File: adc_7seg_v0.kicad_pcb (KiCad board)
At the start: 4 copper layers, 34 parts, among them J1 IN, J2 DC, Q1 BC847, U1 MC78M09C, U2 ICL7106, U3 TDSR1350, U4 TDSR1350, U5 TDSR1350

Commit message: Deployed the remaining parts RC
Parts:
- C3, C6, C7, C8, C9, JP4, Q1, R10, R11, R12: moved to B.Cu
- moved R12 37.3 mm to (192.4, 91.8), turned to 90 degrees
- moved R13 34.5 mm to (220.7, 88.3), turned to 270 degrees
- moved C3 31.3 mm to (210.4, 88.1), turned to 180 degrees
- moved C6 29.6 mm to (221.1, 98.2), turned to 270 degrees
- moved C7 29.0 mm to (224.0, 98.2), turned to 270 degrees
- moved R11 27.1 mm to (210.4, 89.7), turned to 180 degrees
- moved JP4 25.1 mm to (192.4, 94.6)
- moved C8 21.6 mm to (210.4, 91.2), turned to 180 degrees
- moved C9 16.1 mm to (216.7, 98.2), turned to 90 degrees
- moved R10 15.2 mm to (222.6, 98.2), turned to 270 degrees
- moved C5 0.83 mm to (218.9, 97.4)
- moved Q1 0.11 mm to (206.6, 94.2), turned to 90 degrees
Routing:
- net Net-(U2-Pad9): track 17.6 -> 0.00 mm, vias 2 -> 0
- net Net-(U2-Pad10): track 14.4 -> 0.00 mm
- net Net-(U2-Pad21): track 41.5 -> 45.1 mm
- net Net-(U2-Pad25): track 62.7 -> 61.6 mm

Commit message: Revert "Deployed the remaining parts RC"
This reverts commit 7c6476d39b73f4d8eff57732889eea5eef9e1166.
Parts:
- C3, C6, C7, C8, C9, JP4, Q1, R10, R11, R12: moved to F.Cu
- moved R12 37.3 mm to (225.1, 109.6), turned to 0 degrees
- moved R13 34.5 mm to (212.1, 121.7), turned to 0 degrees
- moved C3 31.3 mm to (214.2, 119.2), turned to 0 degrees
- moved C6 29.6 mm to (204.1, 122.4), turned to 0 degrees
- moved C7 29.0 mm to (208.1, 122.4), turned to 0 degrees
- moved R11 27.1 mm to (229.1, 109.3), turned to 0 degrees
- moved JP4 25.1 mm to (200.5, 118.3)
- moved C8 21.6 mm to (225.1, 107.1), turned to 0 degrees
- moved C9 16.1 mm to (230.3, 106.8), turned to 0 degrees
- moved R10 15.2 mm to (237.4, 101.5), turned to 0 degrees
- moved C5 0.83 mm to (219.7, 97.4)
- moved Q1 0.11 mm to (206.5, 94.2), turned to 0 degrees
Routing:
- net Net-(U2-Pad9): track 0.00 -> 17.6 mm, vias 0 -> 2
- net Net-(U2-Pad10): track 0.00 -> 14.4 mm
- net Net-(U2-Pad21): track 45.1 -> 41.5 mm
- net Net-(U2-Pad25): track 61.6 -> 62.7 mm

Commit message: first pokus backup
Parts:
- U2: footprint Package_QFP:LQFP-44_10x10mm_P0.8mm -> Package_QFP:TQFP-44_10x10mm_P0.8mm
- U3, U4, U5: footprint KLALIB_Display_7Segment:TDSR1350 -> KLALIB_Display_7Segment:TDSR1350_small_pads
- moved U2 24.7 mm to (194.3, 90.5), turned to 180 degrees
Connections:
- U3 pad 8: Net-(U3-Pad8) -> (no net)
- U4 pad 8: Net-(U4-Pad8) -> (no net)
- U5 pad 5: Net-(U5-Pad5) -> (no net)
- U5 pad 8: Net-(U5-Pad8) -> (no net)
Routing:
- net Net-(U2-Pad29): track 67.3 -> 0.00 mm
- net Net-(U2-Pad25): track 62.7 -> 0.00 mm, vias 2 -> 0
- net Net-(U2-Pad24): track 59.7 -> 0.00 mm
- net Net-(U2-Pad31): track 56.9 -> 0.00 mm
- net Net-(U2-Pad22): track 52.8 -> 0.00 mm, vias 2 -> 0
- net Net-(U2-Pad23): track 45.8 -> 0.00 mm
- net Net-(U2-Pad30): track 45.2 -> 0.00 mm, vias 1 -> 0
- net Net-(U2-Pad32): track 42.8 -> 0.00 mm, vias 1 -> 0
- net Net-(U2-Pad21): track 41.5 -> 0.00 mm, vias 2 -> 0
- net Net-(U2-Pad20): track 36.0 -> 0.00 mm
- net Net-(U2-Pad19): track 29.5 -> 0.00 mm
- net Net-(U2-Pad18): track 25.1 -> 0.00 mm
- net Net-(U2-Pad15): track 19.6 -> 0.00 mm, vias 1 -> 0
- net Net-(U2-Pad14): track 19.4 -> 0.00 mm
- net Net-(U2-Pad9): track 17.6 -> 0.00 mm, vias 2 -> 0
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
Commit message: updated gitgnore, some changes, wip
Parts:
- C6, C7, C8, C9, R10, R11: moved to B.Cu
- moved R12 82.5 mm to (142.6, 110.6)
- moved JP4 57.6 mm to (143.1, 113.4)
- moved R10 53.5 mm to (184.5, 94.1), turned to 180 degrees
- moved C9 49.6 mm to (185.0, 86.5), turned to 270 degrees
- moved R11 44.5 mm to (193.3, 82.9)
- moved R13 42.6 mm to (219.6, 79.8)
- moved C8 41.2 mm to (193.2, 81.0)
- moved C6 36.0 mm to (184.5, 92.1), turned to 180 degrees
- moved C7 35.8 mm to (184.2, 95.6), turned to 180 degrees
- moved C5 35.4 mm to (185.1, 89.9), turned to 90 degrees
- moved C3 24.5 mm to (218.4, 95.0)
- moved U2 1.46 mm to (192.8, 90.5), turned to 270 degrees
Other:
- net class Default: clearance 0.2 -> 0.254; trace_width 0.25 -> 0.254
- rule trace_clearance: 0.2 -> 0.254

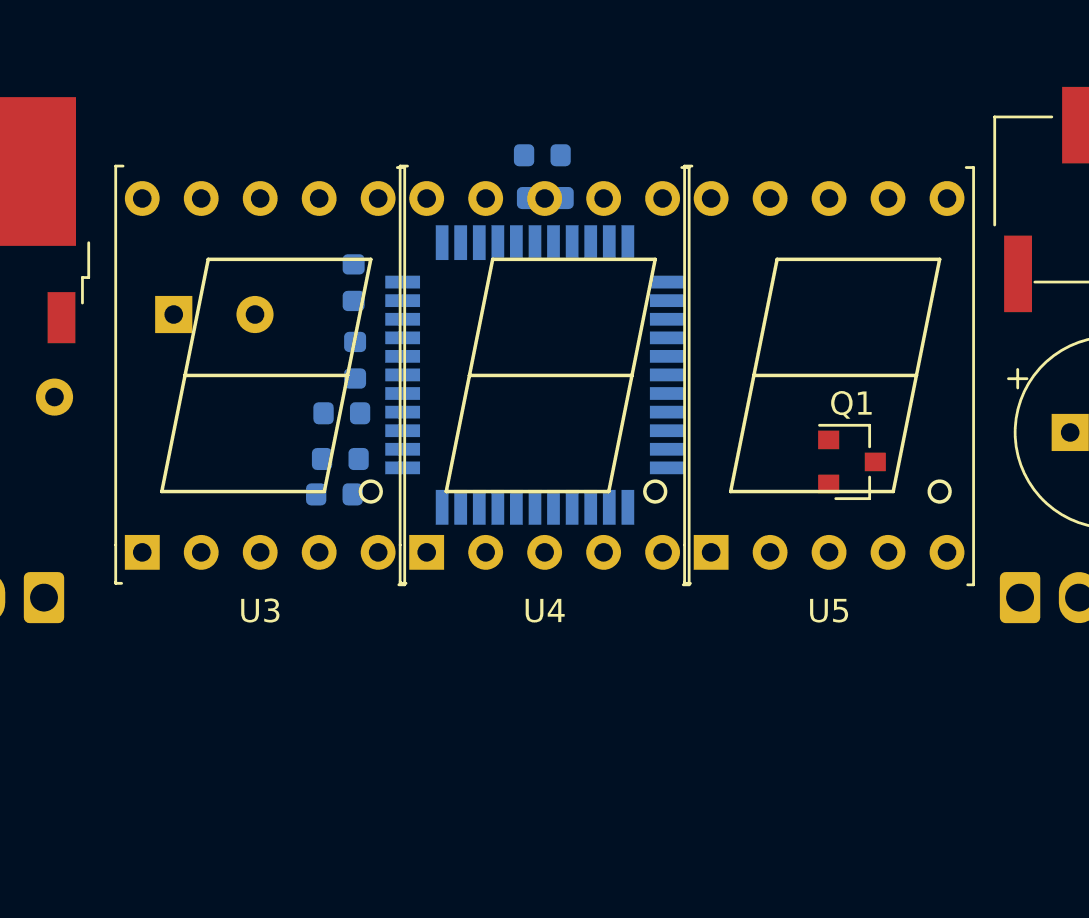
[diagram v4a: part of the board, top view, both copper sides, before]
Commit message: first pokus most of via
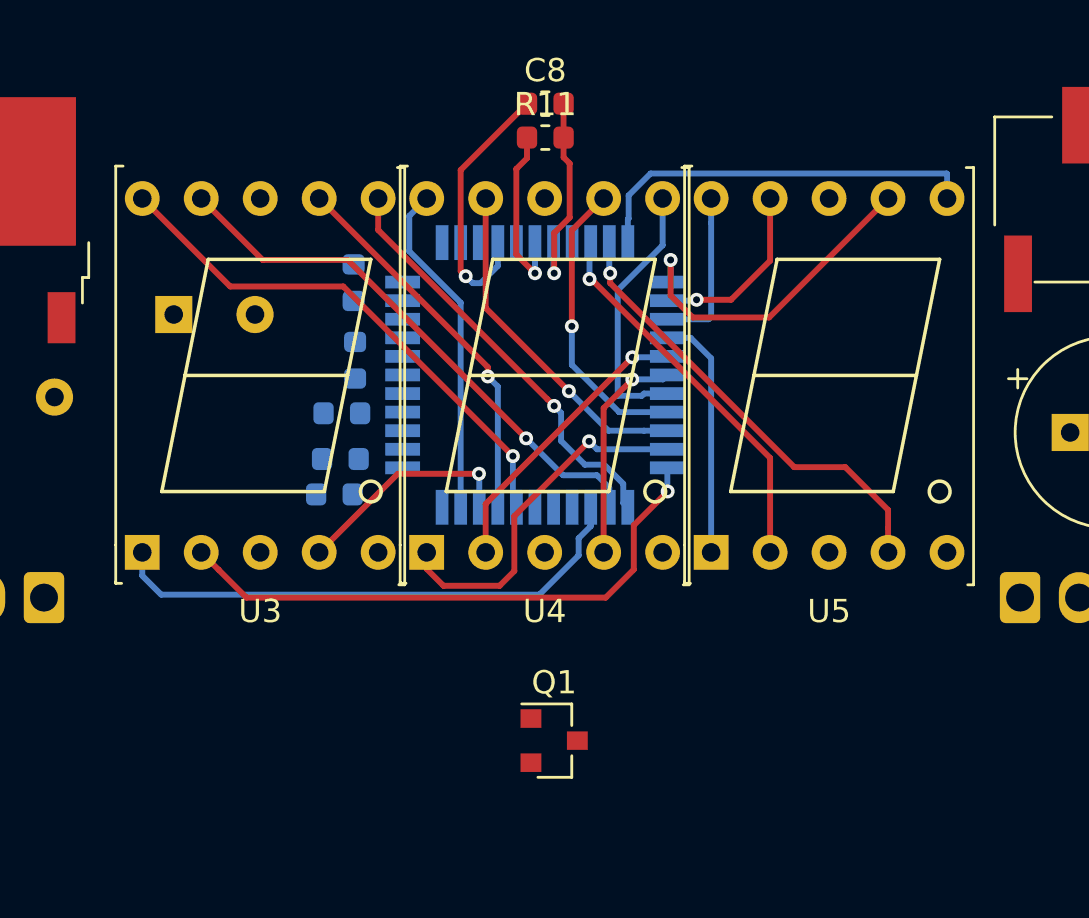
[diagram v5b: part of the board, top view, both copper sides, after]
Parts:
- C8, R11: moved to F.Cu
- moved Q1 17.6 mm to (193.7, 106.2)
- moved R11 2.60 mm to (193.3, 80.3)
- moved C8 2.23 mm to (193.3, 78.8)
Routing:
- net Net-(U2-Pad22): track 0.00 -> 24.9 mm, vias 0 -> 1
- net Net-(U2-Pad24): track 0.00 -> 23.6 mm, vias 0 -> 1
- net Net-(U2-Pad25): track 0.00 -> 23.1 mm
- net Net-(U2-Pad29): track 0.00 -> 22.8 mm, vias 0 -> 1
- net Net-(U2-Pad10): track 0.00 -> 19.6 mm, vias 0 -> 1
- net Net-(U2-Pad23): track 0.00 -> 18.2 mm, vias 0 -> 1
- net Net-(U2-Pad11): track 0.00 -> 17.2 mm
- net Net-(U2-Pad9): track 0.00 -> 16.6 mm, vias 0 -> 1
- net Net-(U2-Pad30): track 0.00 -> 16.5 mm, vias 0 -> 1
- net Net-(U2-Pad21): track 0.00 -> 15.5 mm, vias 0 -> 1
- net Net-(U2-Pad20): track 0.00 -> 14.7 mm, vias 0 -> 1
- net Net-(U2-Pad32): track 0.00 -> 14.5 mm
- net Net-(U2-Pad12): track 0.00 -> 14.4 mm, vias 0 -> 1
- net Net-(U2-Pad19): track 0.00 -> 12.7 mm, vias 0 -> 1
- net Net-(U2-Pad16): track 0.00 -> 12.5 mm, vias 0 -> 1
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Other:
- net class Default: clearance 0.254 -> 0.2
- rule trace_clearance: 0.254 -> 0.2

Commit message: almost last version 0.2.2
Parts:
- removed C4: 100u, Capacitor_THT:CP_Radial_D8.0mm_P3.50mm
- JP1, JP2, JP3: footprint Jumper:SolderJumper-2_P1.3mm_Open_Pad1.0x1.5mm -> KLIB_Mechanical:Jumper; moved to B.Cu
- JP4, R1, R12, R13, R2, R3, R4, R5, R6, R7, R8, U1: moved to B.Cu
- RV1: footprint KLALIB_Potenciometer_SMD:Potentiometer_Bourns_3269P_Horizontal -> KLALIB_Potenciometer_SMD:Potentiometer_SRPASSIVES_1801; moved to B.Cu
- moved JP4 51.4 mm to (193.0, 100.8)
- moved R12 47.4 mm to (189.1, 101.9), turned to 180 degrees
- moved R2 42.1 mm to (184.8, 96.0), turned to 0 degrees
- moved R6 40.8 mm to (184.8, 94.6), turned to 0 degrees
- moved R5 40.0 mm to (184.1, 92.3), turned to 270 degrees
- moved R7 39.3 mm to (188.1, 94.7), turned to 0 degrees
- moved R1 38.1 mm to (185.6, 92.3), turned to 270 degrees
- moved JP3 37.7 mm to (187.9, 93.1), turned to 0 degrees
- moved R4 37.5 mm to (184.8, 90.1), turned to 0 degrees
- moved R3 36.6 mm to (184.8, 88.6), turned to 180 degrees
- moved JP2 35.4 mm to (187.9, 91.5), turned to 0 degrees
- moved R13 35.2 mm to (184.7, 84.7), turned to 180 degrees
- moved R8 34.2 mm to (190.6, 90.0), turned to 90 degrees
- moved J1 34.1 mm to (179.8, 96.1), turned to 90 degrees
- moved JP1 33.5 mm to (187.8, 89.4), turned to 0 degrees
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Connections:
- U2 pad 26: Net-(U2-Pad26) -> (no net)
- U2 pad 27: Net-(U2-Pad27) -> (no net)
- U2 pad 3: Net-(U2-Pad3) -> (no net)
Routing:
- net +9V: track 0.00 -> 94.0 mm, vias 0 -> 3
- net Net-(C5-Pad2): track 0.00 -> 35.9 mm
- net Net-(Q1-Pad2): track 0.00 -> 29.0 mm
- net Net-(U2-Pad25): track 23.1 -> 50.4 mm, vias 0 -> 1
- net Net-(U2-Pad18): track 11.5 -> 32.1 mm
- net Net-(U2-Pad14): track 7.02 -> 25.2 mm
- net Net-(U2-Pad22): track 24.9 -> 38.2 mm, vias 1 -> 0
- net Net-(C1-Pad1): track 0.00 -> 13.3 mm
- net Net-(J1-Pad2): track 0.00 -> 12.9 mm
- net Net-(U2-Pad21): track 15.5 -> 27.1 mm
- net Net-(U2-Pad13): track 7.82 -> 19.3 mm, vias 1 -> 0
- net Net-(U2-Pad29): track 22.8 -> 32.1 mm
- net Net-(Q1-Pad1): track 0.00 -> 9.13 mm, vias 0 -> 1
- net Net-(U2-Pad12): track 14.4 -> 5.82 mm, vias 1 -> 0
- net Net-(C8-Pad1): track 11.5 -> 3.05 mm
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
